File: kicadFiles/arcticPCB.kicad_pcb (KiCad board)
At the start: 2 copper layers, 283 x 94.2 mm, 170 parts, among them J1 TYPE-C-31-M12_13, J2 Conn_01x06_Male, J3 Conn_01x06_Male, J5 Conn_01x06_Male, SW1 MXSwitch, SW10 MXSwitch, SW11 MXSwitch, SW12 MXSwitch, SW13 MXSwitch, SW14 MXSwitch, SW15 MXSwitch, SW16 MXSwitch, SW17 MXSwitch, SW18 MXSwitch, SW19 MXSwitch, SW2 MXSwitch, SW20 MXSwitch, SW21 MXSwitch, SW22 MXSwitch, SW23 MXSwitch, SW24 MXSwitch, SW25 MXSwitch, SW26 MXSwitch, SW27 MXSwitch, SW28 MXSwitch, SW29 MXSwitch, SW3 MXSwitch, SW30 MXSwitch, SW31 MXSwitch, SW32 MXSwitch, SW33 MXSwitch, SW34 MXSwitch, SW35 MXSwitch, SW36 MXSwitch, SW37 MXSwitch, SW38 MXSwitch, SW39 MXSwitch, SW4 MXSwitch, SW40 MXSwitch, SW41 MXSwitch, SW42 MXSwitch, SW43 MXSwitch, SW44 MXSwitch, SW45 MXSwitch, SW46 MXSwitch, SW47 MXSwitch, SW48 MXSwitch, SW49 MXSwitch, SW5 MXSwitch, SW50 MXSwitch, SW51 MXSwitch, SW52 MXSwitch, SW53 MXSwitch, SW54 MXSwitch, SW55 MXSwitch, SW56 MXSwitch, SW57 MXSwitch, SW58 MXSwitch, SW59 MXSwitch, SW6 MXSwitch, SW60 MXSwitch, SW61 MXSwitch, SW62 MXSwitch, SW63 MXSwitch, SW64 MXSwitch, SW65 MXSwitch, SW7 MXSwitch, SW8 MXSwitch, SW9 MXSwitch, U1 STM32F072-LQFP48, U2 USBLC6-2SC6, U3 MCP1700-3302E_SOT23

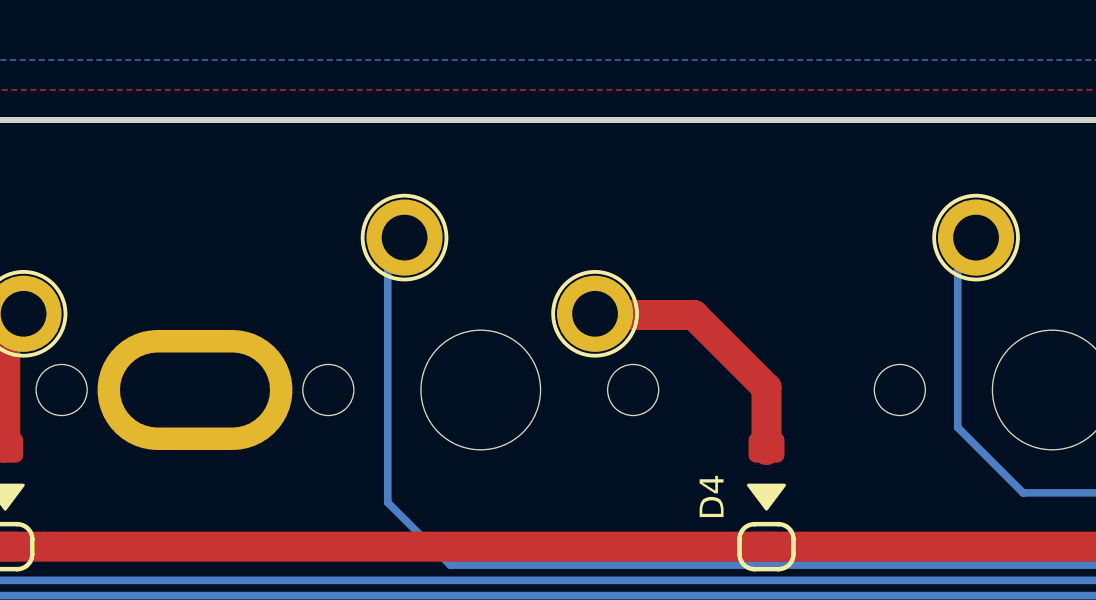
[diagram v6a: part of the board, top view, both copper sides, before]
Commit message: [Update] Added mounting holes ESD protection
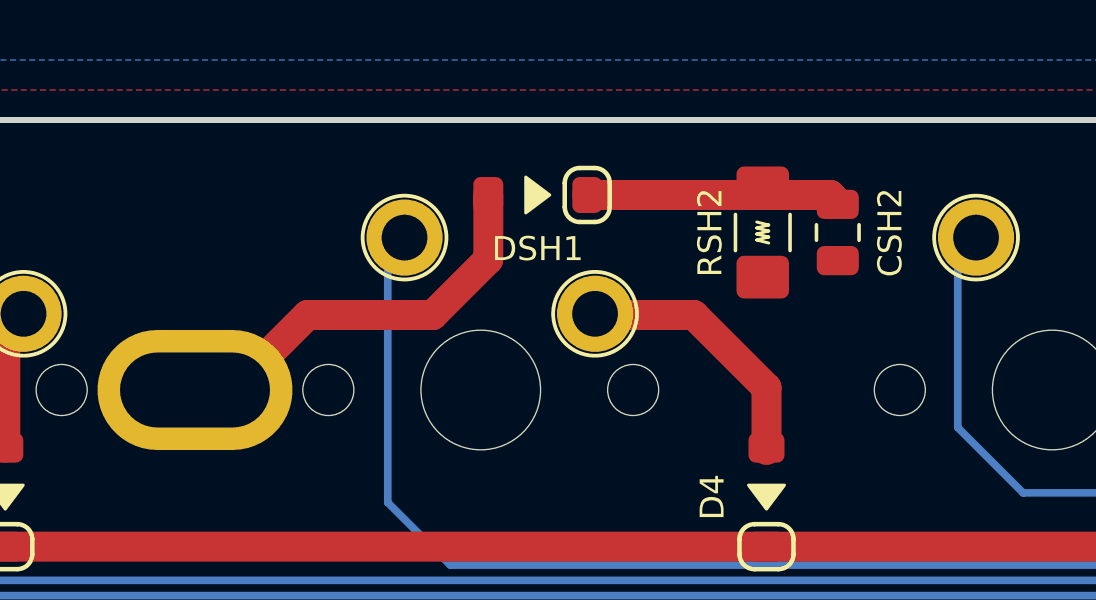
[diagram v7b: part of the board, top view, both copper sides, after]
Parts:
- added CSH2: 4.7nF, Capacitor_SMD:C_0805_2012Metric, F.Cu at (230.6, 3.95)
- added DSH1: 1N4007, acheron_Components:D_SOD-123, F.Cu at (220.6, 2.70)
- added RSH2: 1M, acheron_Components:R_SMD_1026, F.Cu at (228.1, 3.95)
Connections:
- H8 pad 1: (no net) -> CASE
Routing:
- net CASE: track 0.00 -> 13.7 mm
- net Net-(CSH2-Pad2): track 0.00 -> 8.45 mm
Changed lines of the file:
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@@
     (thickness 1.6)
     (drawings 75)
-    (tracks 1582)
+    (tracks 1589)
     (zones 0)
-    (modules 170)
-    (nets 113)
+    (modules 173)
+    (nets 115)
   )
   (page A3)
@@
   )
   (setup
-    (last_trace_width 0.254)
+    (last_trace_width 1)
     (user_trace_width 0.254)
     (user_trace_width 0.5)
@@
   (net 111 J3_2)
   (net 112 J3_1)
+  (net 113 CASE)
+  (net 114 "Net-(CSH2-Pad2)")
   (net_class Default "This is the default net class."
     (clearance 0.127)
@@
     (add_net 5V)
     (add_net BOOT0)
+    (add_net CASE)
     (add_net Col1)
     (add_net Col10)
@@
     (add_net J3_6)
     (add_net NRST)
+    (add_net "Net-(CSH2-Pad2)")
     (add_net "Net-(D1-Pad2)")
     (add_net "Net-(D10-Pad2)")
@@
     (add_net VBUS)
   )
+  (module acheron_Components:R_SMD_1026 (layer F.Cu)
+    (at 228.1 3.95 270)
+    (descr "Resistor SMD 1206 (3216 Metric), square (rectangular) end terminal, IPC_7351 nominal with elongated pad for handsoldering. (Body size source: http://www.tortai-tech.com/upload/download/2011102023233369053.pdf), generated with kicad-footprint-generator")
+    (tags "resistor handsolder")
+    (attr smd)
+    (fp_text reference RSH2 (at 0 1.75 90) (layer F.SilkS)
+      (effects (font (size 0.8 0.8) (thickness 0.2)))
+    )
+    (fp_text value 1M (at 0 2 90) (layer F.Fab)
+      (effects (font (size 0.6 0.6) (thickness 0.1)))
+    )
+    (fp_line (start 0.25 0.2) (end 0.35 -0.2) (layer F.SilkS) (width 0.1))
+    (fp_line (start 0.15 -0.2) (end 0.25 0.2) (layer F.SilkS) (width 0.1))
+    (fp_line (start 0.05 0.2) (end 0.15 -0.2) (layer F.SilkS) (width 0.1))
+    (fp_line (start -0.05 -0.2) (end 0.05 0.2) (layer F.SilkS) (width 0.1))
+    (fp_line (start -0.15 0.2) (end -0.05 -0.2) (layer F.SilkS) (width 0.1))
+    (fp_line (start -0.25 -0.2) (end -0.15 0.2) (layer F.SilkS) (width 0.1))
+    (fp_line (start -0.35 0.2) (end -0.25 -0.2) (layer F.SilkS) (width 0.1))
+    (fp_text user %R (at 0 0 90) (layer F.Fab)
+      (effects (font (size 0.6 0.6) (thickness 0.15)))
+    )
+    (fp_line (start 2.45 1.12) (end -2.45 1.12) (layer F.CrtYd) (width 0.05))
+    (fp_line (start 2.45 -1.12) (end 2.45 1.12) (layer F.CrtYd) (width 0.05))
+    (fp_line (start -2.45 -1.12) (end 2.45 -1.12) (layer F.CrtYd) (width 0.05))
+    (fp_line (start -2.45 1.12) (end -2.45 -1.12) (layer F.CrtYd) (width 0.05))
+    (fp_line (start -0.602064 0.91) (end 0.602064 0.91) (layer F.SilkS) (width 0.12))
+    (fp_line (start -0.602064 -0.91) (end 0.602064 -0.91) (layer F.SilkS) (width 0.12))
+    (fp_line (start 1.6 0.8) (end -1.6 0.8) (layer F.Fab) (width 0.1))
+    (fp_line (start 1.6 -0.8) (end 1.6 0.8) (layer F.Fab) (width 0.1))
+    (fp_line (start -1.6 -0.8) (end 1.6 -0.8) (layer F.Fab) (width 0.1))
+    (fp_line (start -1.6 0.8) (end -1.6 -0.8) (layer F.Fab) (width 0.1))
+    (pad 2 smd roundrect (at 1.4875 0 270) (size 1.425 1.75) (layers F.Cu F.Paste F.Mask) (roundrect_rratio 0.175439)
+      (net 2 GND))
+    (pad 1 smd roundrect (at -1.4875 0 270) (size 1.425 1.75) (layers F.Cu F.Paste F.Mask) (roundrect_rratio 0.175439)
+      (net 114 "Net-(CSH2-Pad2)"))
+    (model ${KISYS3DMOD}/Resistor_SMD.3dshapes/R_1206_3216Metric.wrl
+      (at (xyz 0 0 0))
+      (scale (xyz 1 1 1))
+      (rotate (xyz 0 0 0))
+    )
+  )
+  (module acheron_Components:D_SOD-123 (layer F.Cu)
+    (at 220.6 2.7 180)
+    (descr SOD-123)
+    (tags SOD-123)
+    (attr smd)
+    (fp_text reference DSH1 (at 0 -1.8 180) (layer F.SilkS)
+      (effects (font (size 0.8 0.8) (thickness 0.2)))
+    )
+    (fp_text value 1N4007 (at 0 1.524) (layer F.Fab)
+      (effects (font (size 0.5 0.5) (thickness 0.125)))
+    )
+    (fp_text user A (at 2 0) (layer F.Fab)
+      (effects (font (size 1 1) (thickness 0.15)))
+    )
+    (fp_text user K (at -2 0) (layer F.Fab)
+      (effects (font (size 1 1) (thickness 0.15)))
+    )
+    (fp_poly (pts (xy -0.4 0) (xy 0.4 -0.6) (xy 0.4 0.6)) (layer F.SilkS) (width 0.1))
+    (fp_line (start -1.400038 0.9) (end -1.9 0.9) (layer F.SilkS) (width 0.15))
+    (fp_arc (start -1.4 0.4) (end -1.4 0.9) (angle -90) (layer F.SilkS) (width 0.15))
+    (fp_arc (start -1.9 0.4) (end -2.4 0.4) (angle -90) (layer F.SilkS) (width 0.15))
+    (fp_line (start -2.4 -0.4) (end -2.4 0.4) (layer F.SilkS) (width 0.15))
+    (fp_arc (start -1.9 -0.4) (end -1.9 -0.9) (angle -90) (layer F.SilkS) (width 0.15))
+    (fp_line (start -1.899962 -0.9) (end -1.4 -0.9) (layer F.SilkS) (width 0.15))
+    (fp_line (start -0.9 -0.4) (end -0.9 0.4) (layer F.SilkS) (width 0.15))
+    (fp_arc (start -1.4 -0.4) (end -0.9 -0.4) (angle -90) (layer F.SilkS) (width 0.15))
+    (fp_line (start -2.35 -1.15) (end -2.35 1.15) (layer F.CrtYd) (width 0.05))
+    (fp_line (start 2.35 1.15) (end -2.35 1.15) (layer F.CrtYd) (width 0.05))
+    (fp_line (start 2.35 -1.15) (end 2.35 1.15) (layer F.CrtYd) (width 0.05))
+    (fp_line (start -2.35 -1.15) (end 2.35 -1.15) (layer F.CrtYd) (width 0.05))
+    (fp_line (start -1.4 -0.9) (end 1.4 -0.9) (layer F.Fab) (width 0.1))
+    (fp_line (start 1.4 -0.9) (end 1.4 0.9) (layer F.Fab) (width 0.1))
+    (fp_line (start 1.4 0.9) (end -1.4 0.9) (layer F.Fab) (width 0.1))
+    (fp_line (start -1.4 0.9) (end -1.4 -0.9) (layer F.Fab) (width 0.1))
+    (fp_line (start -0.75 0) (end -0.35 0) (layer F.Fab) (width 0.1))
+    (fp_line (start -0.35 0) (end -0.35 -0.55) (layer F.Fab) (width 0.1))
+    (fp_line (start -0.35 0) (end -0.35 0.55) (layer F.Fab) (width 0.1))
+    (fp_line (start -0.35 0) (end 0.25 -0.4) (layer F.Fab) (width 0.1))
+    (fp_line (start 0.25 -0.4) (end 0.25 0.4) (layer F.Fab) (width 0.1))
+    (fp_line (start 0.25 0.4) (end -0.35 0) (layer F.Fab) (width 0.1))
+    (fp_line (start 0.25 0) (end 0.75 0) (layer F.Fab) (width 0.1))
+    (fp_text user %R (at 0 -1.397) (layer F.Fab)
+      (effects (font (size 0.5 0.5) (thickness 0.125)))
+    )
+    (pad 2 smd roundrect (at 1.65 0 180) (size 1 1.2) (layers F.Cu F.Paste F.Mask) (roundrect_rratio 0.25)
+      (net 113 CASE))
+    (pad 1 smd roundrect (at -1.65 0 180) (size 1 1.2) (layers F.Cu F.Paste F.Mask) (roundrect_rratio 0.25)
+      (net 114 "Net-(CSH2-Pad2)"))
+    (model ${KISYS3DMOD}/Diode_SMD.3dshapes/D_SOD-123.wrl
+      (at (xyz 0 0 0))
+      (scale (xyz 1 1 1))
+      (rotate (xyz 0 0 0))
+    )
+  )
+  (module Capacitor_SMD:C_0805_2012Metric (layer F.Cu)
+    (at 230.6 3.95 90)
+    (descr "Capacitor SMD 0805 (2012 Metric), square (rectangular) end terminal, IPC_7351 nominal, (Body size source: https://docs.google.com/spreadsheets/d/1BsfQQcO9C6DZCsRaXUlFlo91Tg2WpOkGARC1WS5S8t0/edit?usp=sharing), generated with kicad-footprint-generator")
+    (tags capacitor)
+    (attr smd)
+    (fp_text reference CSH2 (at 0 1.75 90) (layer F.SilkS)
+      (effects (font (size 0.8 0.8) (thickness 0.2)))
+    )
+    (fp_text value 4.7nF (at 0 1.65 90) (layer F.Fab)
+      (effects (font (size 1 1) (thickness 0.15)))
+    )
+    (fp_text user %R (at 0 0 90) (layer F.Fab)
+      (effects (font (size 0.5 0.5) (thickness 0.08)))
+    )
+    (fp_line (start 1.68 0.95) (end -1.68 0.95) (layer F.CrtYd) (width 0.05))
+    (fp_line (start 1.68 -0.95) (end 1.68 0.95) (layer F.CrtYd) (width 0.05))
+    (fp_line (start -1.68 -0.95) (end 1.68 -0.95) (layer F.CrtYd) (width 0.05))
+    (fp_line (start -1.68 0.95) (end -1.68 -0.95) (layer F.CrtYd) (width 0.05))
+    (fp_line (start -0.258578 0.71) (end 0.258578 0.71) (layer F.SilkS) (width 0.12))
+    (fp_line (start -0.258578 -0.71) (end 0.258578 -0.71) (layer F.SilkS) (width 0.12))
+    (fp_line (start 1 0.6) (end -1 0.6) (layer F.Fab) (width 0.1))
+    (fp_line (start 1 -0.6) (end 1 0.6) (layer F.Fab) (width 0.1))
+    (fp_line (start -1 -0.6) (end 1 -0.6) (layer F.Fab) (width 0.1))
+    (fp_line (start -1 0.6) (end -1 -0.6) (layer F.Fab) (width 0.1))
+    (pad 2 smd roundrect (at 0.9375 0 90) (size 0.975 1.4) (layers F.Cu F.Paste F.Mask) (roundrect_rratio 0.25)
+      (net 114 "Net-(CSH2-Pad2)"))
+    (pad 1 smd roundrect (at -0.9375 0 90) (size 0.975 1.4) (layers F.Cu F.Paste F.Mask) (roundrect_rratio 0.25)
+      (net 2 GND))
+    (model ${KISYS3DMOD}/Capacitor_SMD.3dshapes/C_0805_2012Metric.wrl
+      (at (xyz 0 0 0))
+      (scale (xyz 1 1 1))
+      (rotate (xyz 0 0 0))
+    )
+  )
   (module acheron_MX:MX100 (layer F.Cu)
     (at 247.27488 28.25008)
@@
     )
     (pad 1 thru_hole oval (at 0 0) (size 6.5 4) (drill oval 5 2.5) (layers *.Cu *.Mask)
-      (clearance 1))
+      (net 113 CASE) (clearance 1))
     (model cherry_mx1.wrl
       (at (xyz 0 0 0))
@@
   (segment (start 264.00802 44.076114) (end 264.00802 41.468178) (width 0.254) (layer F.Cu) (net 112))
   (segment (start 279.75 46) (end 279.75 43.2) (width 0.254) (layer F.Cu) (net 112))
+  (segment (start 210.42472 9.2) (end 209.17472 9.2) (width 1) (layer F.Cu) (net 113))
+  (segment (start 212.92472 6.7) (end 210.42472 9.2) (width 1) (layer F.Cu) (net 113))
+  (segment (start 218.95 2.7) (end 218.95 4.85) (width 1) (layer F.Cu) (net 113))
+  (segment (start 217.1 6.7) (end 212.92472 6.7) (width 1) (layer F.Cu) (net 113))
+  (segment (start 218.95 4.85) (end 217.1 6.7) (width 1) (layer F.Cu) (net 113))
+  (segment (start 222.25 2.7) (end 230.35 2.7) (width 1) (layer F.Cu) (net 114))
+  (segment (start 230.35 2.7) (end 230.6 2.95) (width 1) (layer F.Cu) (net 114))
   (zone (net 0) (net_name "") (layer F.Cu) (hatch edge 0.508)
     (connect_pads (clearance 0.508))

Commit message: Added RCC2
- The PCB used a single pulldown resistor for both CC1 and CC2 pins of the USB connector, which is not the right way to do it. This has been fixed and now each CC pin has a single resistor.
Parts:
- added RCC2: 5.1k, acheron_Components:R_SMD_1026, F.Cu at (260.4, 14.9)
- moved RCC1 1.46 mm to (260.4, 12.5)
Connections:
- J1 pad B5: Net-(J1-PadA5) -> Net-(J1-PadB5)
- RCC1 pad 2: Net-(J1-PadA5) -> Net-(J1-PadB5)
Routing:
- net Net-(J1-PadB5): track 0.00 -> 8.79 mm
- net Net-(J1-PadA5): track 20.7 -> 14.0 mm
- net Col12: track 568.4 -> 565.2 mm
- net Col11: track 606.0 -> 603.1 mm
- net Col10: track 609.0 -> 606.2 mm
- net Row2: track 278.2 -> 278.7 mm
